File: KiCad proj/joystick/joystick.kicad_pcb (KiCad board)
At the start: 2 copper layers, 33 parts, among them J1 Joystic_conn, J2 USB_conn, J3 Keyboard_conn, J4 SWD, Q1 Q_PNP_BEC, U1 STM32F103C8Tx, U2 NCP500SN33T1, Y1 16MHz

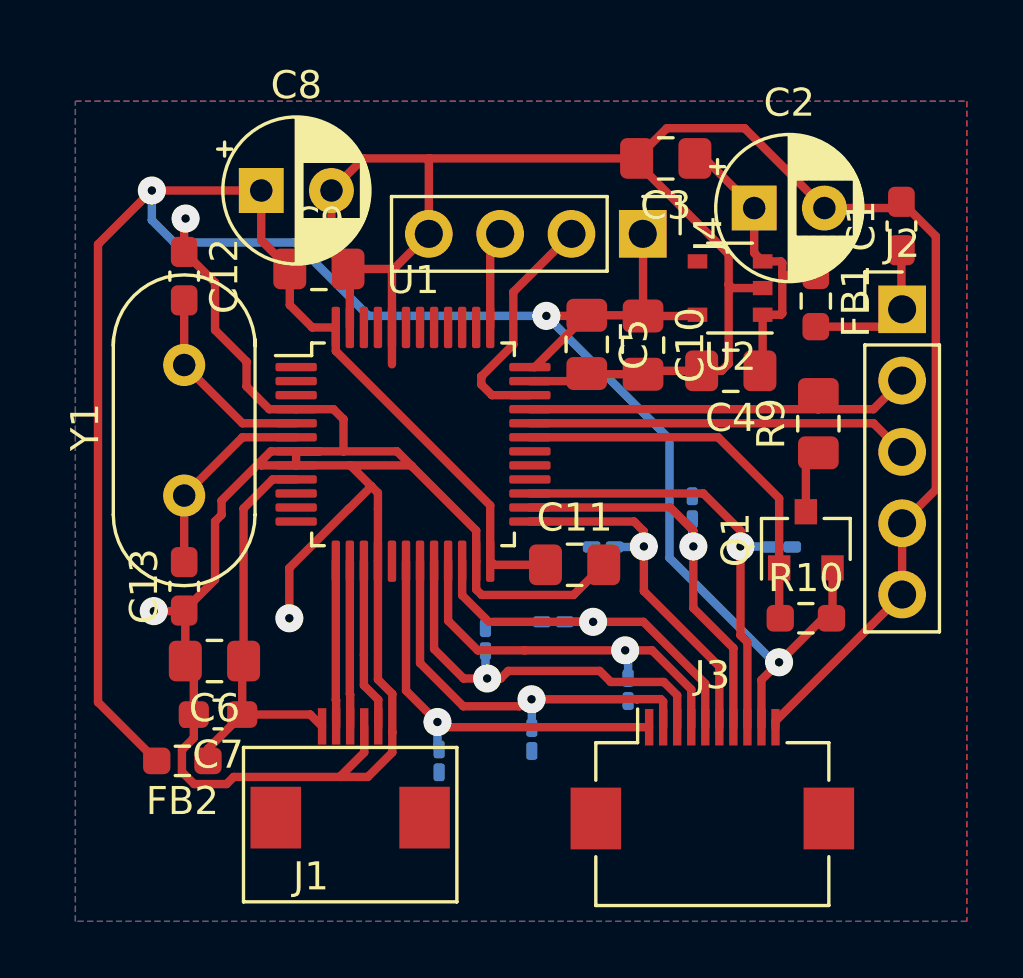
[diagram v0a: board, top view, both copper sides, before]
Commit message: Add new joystick shcematics
Add schematics for keyboard and jouystick adaptors
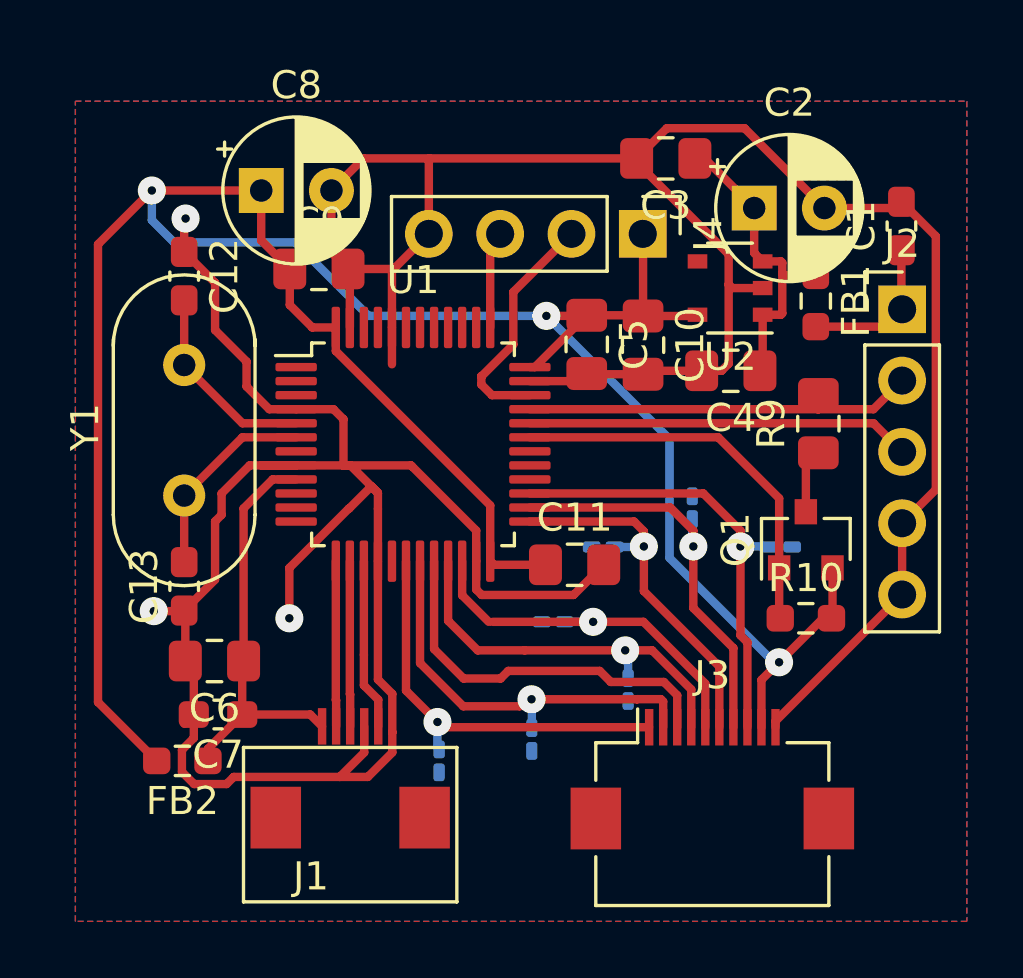
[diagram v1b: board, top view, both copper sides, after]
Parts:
- removed R3: 10k, Resistor_SMD:R_0201_0603Metric_Pad0.64x0.40mm_HandSolder
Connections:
- net 3.3 renamed 3,3Vdd
- U1 pad 7: Gnd -> Net-(U1-Pad7)
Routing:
- net Gnd: track 153.2 -> 148.4 mm
- net Net-(J3-Pad3): track 14.8 -> 13.8 mm, vias 1 -> 0
